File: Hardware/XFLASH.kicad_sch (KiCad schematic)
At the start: 0 parts

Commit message: Checkpoint
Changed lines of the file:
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@@
 (kicad_sch (version 20230121) (generator eeschema)
   (paper "A4")
-  (hierarchical_label "SCK" (shape input) (at 127 35.56 0) (fields_autoplaced)
+  (bus (pts (xy 241.3 25.4) (xy 266.7 25.4))
+    (stroke (width 0) (type default))
+  )
+  (label "IO[0..3]" (at 241.3 25.4 0) (fields_autoplaced)
+    (effects (font (size 1.27 1.27)) (justify left bottom))
+  )
+  (hierarchical_label "CLK" (shape input) (at 127 35.56 0) (fields_autoplaced)
     (effects (font (size 1.27 1.27)) (justify left))
   )
-  (hierarchical_label "IO1" (shape bidirectional) (at 127 43.18 0) (fields_autoplaced)
+  (hierarchical_label "VCC" (shape passive) (at 127 45.72 0) (fields_autoplaced)
     (effects (font (size 1.27 1.27)) (justify left))
   )
-  (hierarchical_label "IO3" (shape bidirectional) (at 127 48.26 0) (fields_autoplaced)
+  (hierarchical_label "IO[0..3]" (shape bidirectional) (at 266.7 25.4 0) (fields_autoplaced)
     (effects (font (size 1.27 1.27)) (justify left))
   )
-  (hierarchical_label "IO0" (shape bidirectional) (at 127 40.64 0) (fields_autoplaced)
+  (hierarchical_label "~{CS}" (shape input) (at 127 38.1 0) (fields_autoplaced)
     (effects (font (size 1.27 1.27)) (justify left))
   )
-  (hierarchical_label "~{NSS}" (shape input) (at 127 38.1 0) (fields_autoplaced)
-    (effects (font (size 1.27 1.27)) (justify left))
-  )
-  (hierarchical_label "IO2" (shape bidirectional) (at 127 45.72 0) (fields_autoplaced)
-    (effects (font (size 1.27 1.27)) (justify left))
-  )

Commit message: Checkpoint
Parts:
- added C25: 100nF, symbol Device:C_Small
- added R18, R19, R20: 10K, symbol Device:R_Small
- added U6: IS25LP064A-JBLE, Package_SO:SOIC-8_5.23x5.23mm_P1.27mm, symbol Memory_Flash:W25Q128JVS
- added U8: W25Q128JVPM, Package_SON:WSON-8-1EP_6x5mm_P1.27mm_EP3.4x4.3mm, symbol Memory_Flash:W25Q32JVZP
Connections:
- net CLK: now also U6.6 (CLK), U8.6 (CLK)
- net VCC: now also C25.1, R18.1, R19.1, R20.1, U6.8 (VCC), U8.8 (VCC)
- net ~{CS}: now also R18.2, U6.1 (~{CS}), U8.1 (~{CS})
- new net GND: C25.2, U6.4 (GND), U8.4 (GND), U8.9 (EP)
- new net IO0: U6.5 (DI(IO0)), U8.5 (DI(IO0))
- new net IO1: U6.2 (DO(IO1)), U8.2 (DO(IO1))
- new net IO2: R19.2, U6.3 (IO2), U8.3 (IO2)
- new net IO3: R20.2, U6.7 (IO3), U8.7 (IO3)

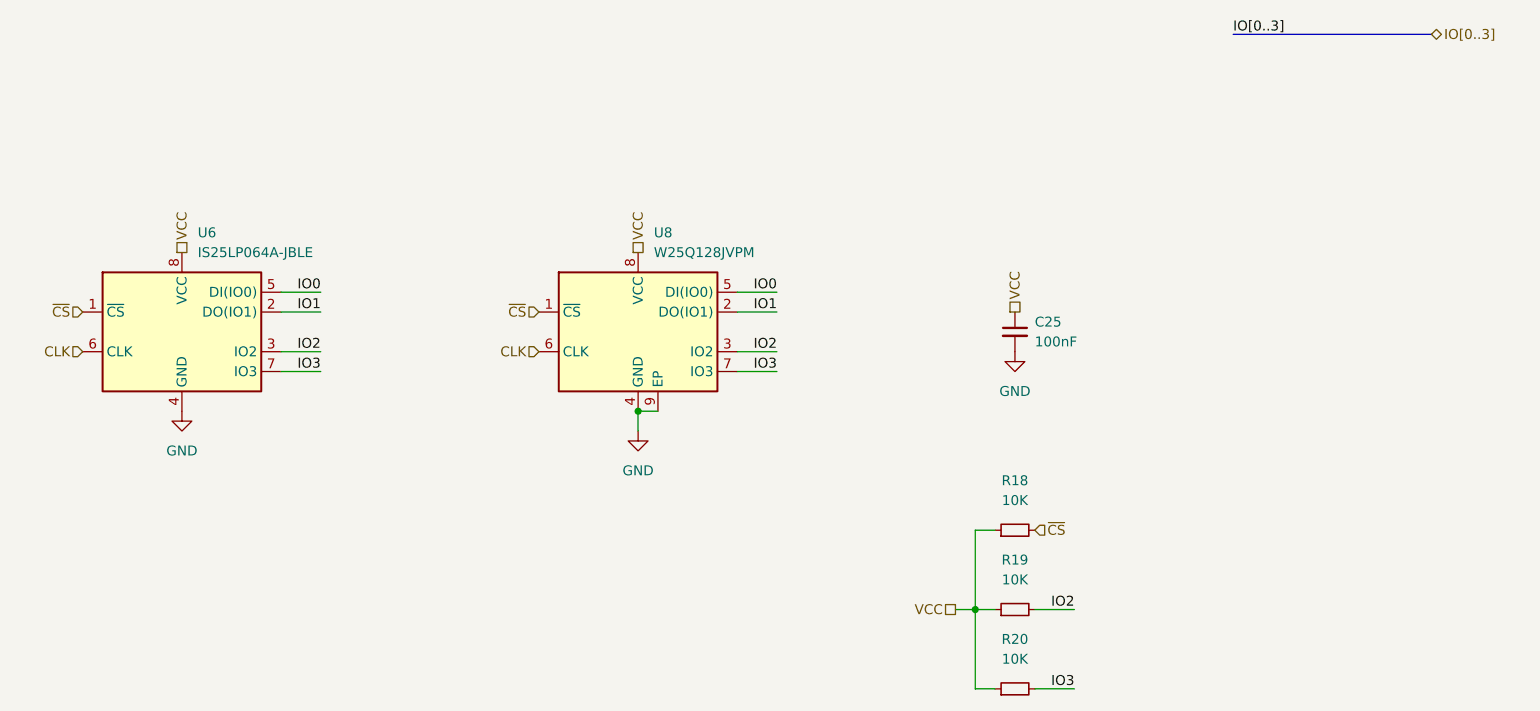
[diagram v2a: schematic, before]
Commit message: Add stacked footprints graphic
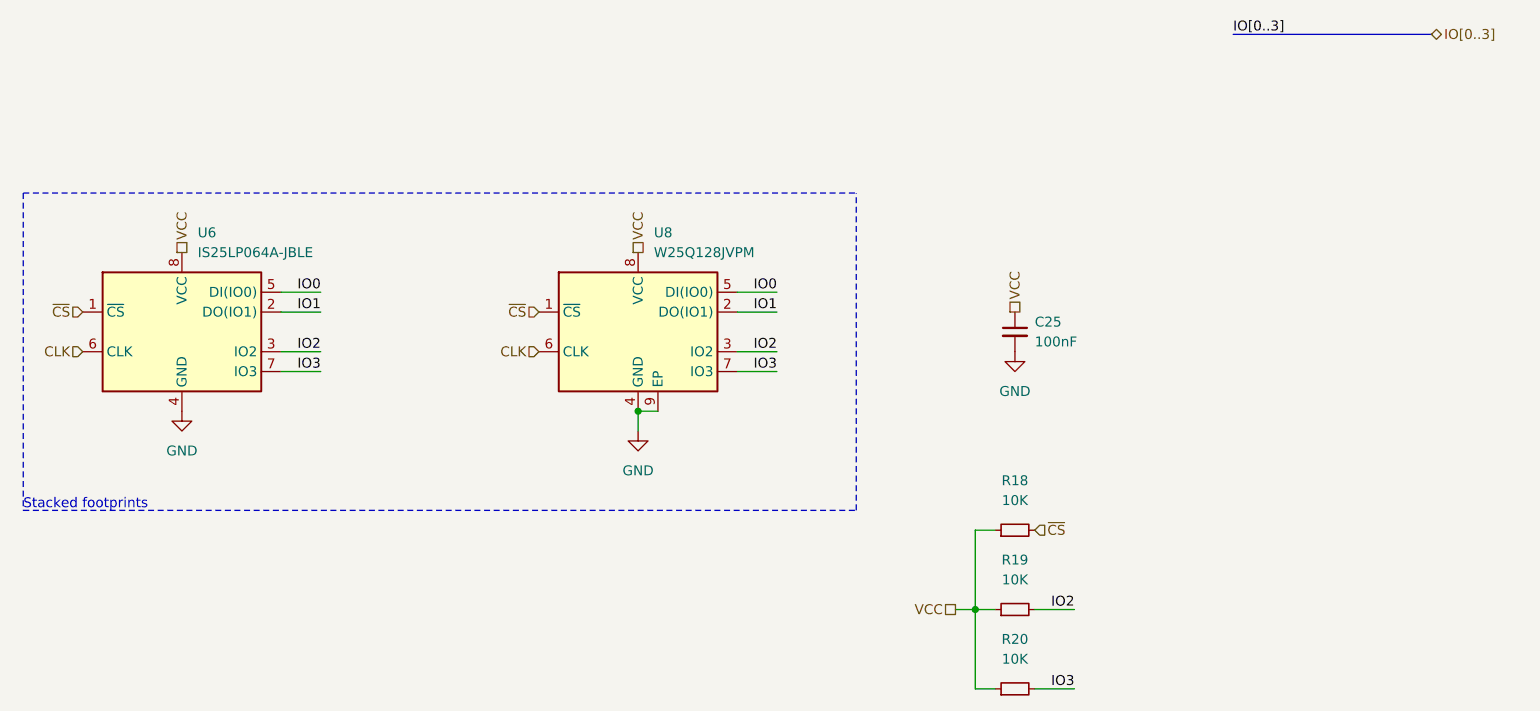
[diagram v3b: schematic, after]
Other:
- note added: "Stacked footprints"
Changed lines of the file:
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@@
   (junction (at 165.1 73.66) (diameter 0) (color 0 0 0 0)
+  )
+  (polyline (pts (xy 193.04 86.36) (xy 193.04 45.72))
+    (stroke (width 0) (type dash))
   )
   (wire (pts (xy 208.28 109.22) (xy 210.82 109.22))
@@
     (stroke (width 0) (type default))
   )
+  (polyline (pts (xy 86.36 45.72) (xy 86.36 86.36))
+    (stroke (width 0) (type dash))
+  )
   (wire (pts (xy 208.28 88.9) (xy 210.82 88.9))
     (stroke (width 0) (type default))
@@
   (wire (pts (xy 165.1 73.66) (xy 165.1 76.2))
     (stroke (width 0) (type default))
+  )
+  (polyline (pts (xy 86.36 86.36) (xy 193.04 86.36))
+    (stroke (width 0) (type dash))
   )
   (wire (pts (xy 215.9 99.06) (xy 220.98 99.06))
@@
   (bus (pts (xy 241.3 25.4) (xy 266.7 25.4))
     (stroke (width 0) (type default))
+  )
+  (polyline (pts (xy 86.36 45.72) (xy 193.04 45.72))
+    (stroke (width 0) (type dash))
   )
   (wire (pts (xy 208.28 99.06) (xy 208.28 109.22))
@@
     (stroke (width 0) (type default))
   )
+  (text "Stacked footprints" (at 86.36 86.36 0)
+    (effects (font (size 1.27 1.27)) (justify left bottom))
+  )
   (label "IO2" (at 220.98 99.06 180) (fields_autoplaced)

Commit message: ERC fixes
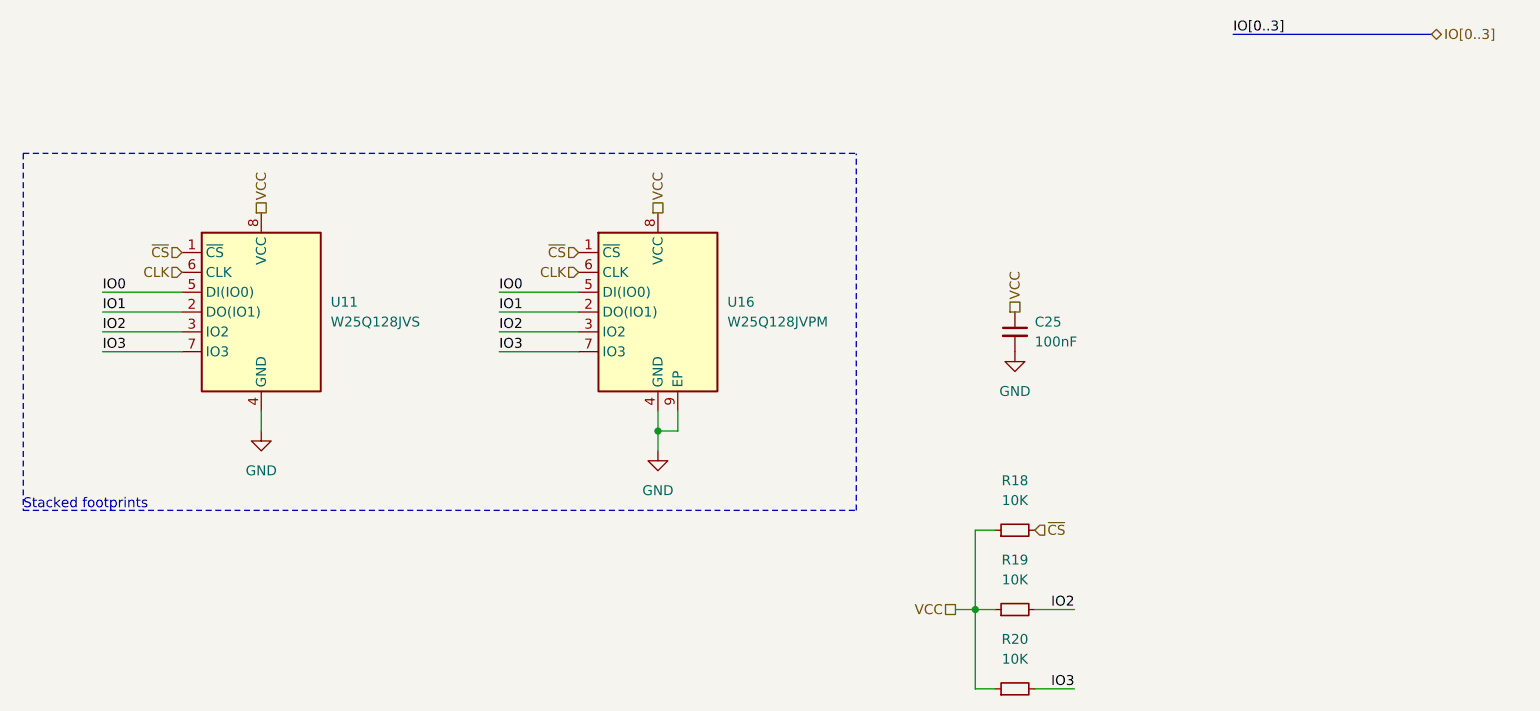
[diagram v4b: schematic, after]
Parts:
- removed U6: IS25LP064A-JBLE, Package_SO:SOIC-8_5.23x5.23mm_P1.27mm, symbol Memory_Flash:W25Q128JVS
- removed U8: W25Q128JVPM, Package_SON:WSON-8-1EP_6x5mm_P1.27mm_EP3.4x4.3mm, symbol Memory_Flash:W25Q32JVZP
- added U11: W25Q128JVS, Package_SO:SOIC-8_5.23x5.23mm_P1.27mm, symbol Memory_Flash:W25Q128JVS
- added U16: W25Q128JVPM, Package_SON:WSON-8-1EP_6x5mm_P1.27mm_EP3.4x4.3mm, symbol Memory_Flash:W25Q32JVZP
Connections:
- net CLK: now also U11.6 (CLK), U16.6 (CLK)
- net GND: now also U11.4 (GND), U16.4 (GND), U16.9 (EP)
- net IO0: now also U11.5 (DI(IO0)), U16.5 (DI(IO0))
- net IO1: now also U11.2 (DO(IO1)), U16.2 (DO(IO1))
- net IO2: now also U11.3 (IO2), U16.3 (IO2)
- net IO3: now also U11.7 (IO3), U16.7 (IO3)
- net VCC: now also U11.8 (VCC), U16.8 (VCC)
- net ~{CS}: now also U11.1 (~{CS}), U16.1 (~{CS})

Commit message: Checkpoint
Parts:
- renumbered C25 to C?, R20 to R?, R18 to R?, R19 to R?, U11 to U501, U16 to U502
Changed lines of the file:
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@@
   (symbol (lib_id "Device:R_Small") (at 213.36 109.22 90) (unit 1)
     (in_bom yes) (on_board yes) (dnp no) (fields_autoplaced)
-    (property "Reference" "R20" (at 213.36 102.87 90)
+    (property "Reference" "R?" (at 213.36 102.87 90)
       (effects (font (size 1.27 1.27)))
     )
@@
       (project "STM32_144_dev_board1"
         (path "/687cb9d5-0148-4d02-92a8-2c8817ac4452/5a3f2e83-2524-4987-84b3-442c172b4877"
-          (reference "R20") (unit 1)
-        )
-      )
-      (project "Avionus_Flight_Controller"
-        (path "/ddc7e940-0588-4587-8902-8ced9e615ace/31e99b3b-1804-434d-b69d-c6e432b73a14"
-          (reference "R62") (unit 1)
-        )
-        (path "/ddc7e940-0588-4587-8902-8ced9e615ace/5d37de1e-dde8-47f7-bd31-55135827514e"
-          (reference "R65") (unit 1)
+          (reference "R?") (unit 1)
+        )
+      )
+      (project "Avionus_Flight_Controller"
+        (path "/ddc7e940-0588-4587-8902-8ced9e615ace/31e99b3b-1804-434d-b69d-c6e432b73a14"
+          (reference "R503") (unit 1)
+        )
+        (path "/ddc7e940-0588-4587-8902-8ced9e615ace/5d37de1e-dde8-47f7-bd31-55135827514e"
+          (reference "R603") (unit 1)
         )
       )
@@
   (symbol (lib_id "Device:C_Small") (at 213.36 63.5 0) (unit 1)
     (in_bom yes) (on_board yes) (dnp no) (fields_autoplaced)
-    (property "Reference" "C25" (at 215.9 62.2362 0)
+    (property "Reference" "C?" (at 215.9 62.2362 0)
       (effects (font (size 1.27 1.27)) (justify left))
     )
@@
       (project "STM32_144_dev_board1"
         (path "/687cb9d5-0148-4d02-92a8-2c8817ac4452/5a3f2e83-2524-4987-84b3-442c172b4877"
-          (reference "C25") (unit 1)
-        )
-      )
-      (project "Avionus_Flight_Controller"
-        (path "/ddc7e940-0588-4587-8902-8ced9e615ace/31e99b3b-1804-434d-b69d-c6e432b73a14"
-          (reference "C25") (unit 1)
-        )
-        (path "/ddc7e940-0588-4587-8902-8ced9e615ace/5d37de1e-dde8-47f7-bd31-55135827514e"
-          (reference "C26") (unit 1)
+          (reference "C?") (unit 1)
+        )
+      )
+      (project "Avionus_Flight_Controller"
+        (path "/ddc7e940-0588-4587-8902-8ced9e615ace/31e99b3b-1804-434d-b69d-c6e432b73a14"
+          (reference "C501") (unit 1)
+        )
+        (path "/ddc7e940-0588-4587-8902-8ced9e615ace/5d37de1e-dde8-47f7-bd31-55135827514e"
+          (reference "C601") (unit 1)
         )
       )
@@
   (symbol (lib_id "Memory_Flash:W25Q128JVS") (at 116.84 60.96 0) (unit 1)
     (in_bom yes) (on_board yes) (dnp no) (fields_autoplaced)
-    (property "Reference" "U11" (at 125.73 59.69 0)
+    (property "Reference" "U501" (at 125.73 59.69 0)
       (effects (font (size 1.27 1.27)) (justify left))
     )
@@
       (project "Avionus_Flight_Controller"
         (path "/ddc7e940-0588-4587-8902-8ced9e615ace/31e99b3b-1804-434d-b69d-c6e432b73a14"
-          (reference "U11") (unit 1)
-        )
-        (path "/ddc7e940-0588-4587-8902-8ced9e615ace/5d37de1e-dde8-47f7-bd31-55135827514e"
-          (reference "U13") (unit 1)
+          (reference "U501") (unit 1)
+        )
+        (path "/ddc7e940-0588-4587-8902-8ced9e615ace/5d37de1e-dde8-47f7-bd31-55135827514e"
+          (reference "U601") (unit 1)
         )
       )
@@
   (symbol (lib_name "GND_1") (lib_id "power:GND") (at 116.84 76.2 0) (unit 1)
     (in_bom yes) (on_board yes) (dnp no) (fields_autoplaced)
-    (property "Reference" "#PWR037" (at 116.84 82.55 0)
+    (property "Reference" "#PWR0501" (at 116.84 82.55 0)
       (effects (font (size 1.27 1.27)) hide)
     )
@@
       (project "Avionus_Flight_Controller"
         (path "/ddc7e940-0588-4587-8902-8ced9e615ace/31e99b3b-1804-434d-b69d-c6e432b73a14"
-          (reference "#PWR037") (unit 1)
-        )
-        (path "/ddc7e940-0588-4587-8902-8ced9e615ace/5d37de1e-dde8-47f7-bd31-55135827514e"
-          (reference "#PWR039") (unit 1)
+          (reference "#PWR0501") (unit 1)
+        )
+        (path "/ddc7e940-0588-4587-8902-8ced9e615ace/5d37de1e-dde8-47f7-bd31-55135827514e"
+          (reference "#PWR0601") (unit 1)
         )
       )
@@
   (symbol (lib_id "Device:R_Small") (at 213.36 88.9 90) (unit 1)
     (in_bom yes) (on_board yes) (dnp no) (fields_autoplaced)
-    (property "Reference" "R18" (at 213.36 82.55 90)
+    (property "Reference" "R?" (at 213.36 82.55 90)
       (effects (font (size 1.27 1.27)))
     )
@@
       (project "STM32_144_dev_board1"
         (path "/687cb9d5-0148-4d02-92a8-2c8817ac4452/5a3f2e83-2524-4987-84b3-442c172b4877"
-          (reference "R18") (unit 1)
-        )
-      )
-      (project "Avionus_Flight_Controller"
-        (path "/ddc7e940-0588-4587-8902-8ced9e615ace/31e99b3b-1804-434d-b69d-c6e432b73a14"
-          (reference "R60") (unit 1)
-        )
-        (path "/ddc7e940-0588-4587-8902-8ced9e615ace/5d37de1e-dde8-47f7-bd31-55135827514e"
-          (reference "R63") (unit 1)
+          (reference "R?") (unit 1)
+        )
+      )
+      (project "Avionus_Flight_Controller"
+        (path "/ddc7e940-0588-4587-8902-8ced9e615ace/31e99b3b-1804-434d-b69d-c6e432b73a14"
+          (reference "R501") (unit 1)
+        )
+        (path "/ddc7e940-0588-4587-8902-8ced9e615ace/5d37de1e-dde8-47f7-bd31-55135827514e"
+          (reference "R601") (unit 1)
         )
       )
@@
   (symbol (lib_id "power:GND") (at 213.36 66.04 0) (unit 1)
     (in_bom yes) (on_board yes) (dnp no) (fields_autoplaced)
-    (property "Reference" "#PWR038" (at 213.36 72.39 0)
+    (property "Reference" "#PWR0503" (at 213.36 72.39 0)
       (effects (font (size 1.27 1.27)) hide)
     )
@@
       (project "Avionus_Flight_Controller"
         (path "/ddc7e940-0588-4587-8902-8ced9e615ace/31e99b3b-1804-434d-b69d-c6e432b73a14"
-          (reference "#PWR038") (unit 1)
-        )
-        (path "/ddc7e940-0588-4587-8902-8ced9e615ace/5d37de1e-dde8-47f7-bd31-55135827514e"
-          (reference "#PWR042") (unit 1)
+          (reference "#PWR0503") (unit 1)
+        )
+        (path "/ddc7e940-0588-4587-8902-8ced9e615ace/5d37de1e-dde8-47f7-bd31-55135827514e"
+          (reference "#PWR0603") (unit 1)
         )
       )
@@
   (symbol (lib_name "W25Q32JVZP_1") (lib_id "Memory_Flash:W25Q32JVZP") (at 167.64 60.96 0) (unit 1)
     (in_bom yes) (on_board yes) (dnp no) (fields_autoplaced)
-    (property "Reference" "U16" (at 176.53 59.69 0)
+    (property "Reference" "U502" (at 176.53 59.69 0)
       (effects (font (size 1.27 1.27)) (justify left))
     )
@@
       (project "Avionus_Flight_Controller"
         (path "/ddc7e940-0588-4587-8902-8ced9e615ace/31e99b3b-1804-434d-b69d-c6e432b73a14"
-          (reference "U16") (unit 1)
-        )
-        (path "/ddc7e940-0588-4587-8902-8ced9e615ace/5d37de1e-dde8-47f7-bd31-55135827514e"
-          (reference "U17") (unit 1)
+          (reference "U502") (unit 1)
+        )
+        (path "/ddc7e940-0588-4587-8902-8ced9e615ace/5d37de1e-dde8-47f7-bd31-55135827514e"
+          (reference "U602") (unit 1)
         )
       )
@@
   (symbol (lib_name "GND_1") (lib_id "power:GND") (at 167.64 78.74 0) (unit 1)
     (in_bom yes) (on_board yes) (dnp no) (fields_autoplaced)
-    (property "Reference" "#PWR041" (at 167.64 85.09 0)
+    (property "Reference" "#PWR0502" (at 167.64 85.09 0)
       (effects (font (size 1.27 1.27)) hide)
     )
@@
       (project "Avionus_Flight_Controller"
         (path "/ddc7e940-0588-4587-8902-8ced9e615ace/31e99b3b-1804-434d-b69d-c6e432b73a14"
-          (reference "#PWR041") (unit 1)
-        )
-        (path "/ddc7e940-0588-4587-8902-8ced9e615ace/5d37de1e-dde8-47f7-bd31-55135827514e"
-          (reference "#PWR043") (unit 1)
+          (reference "#PWR0502") (unit 1)
+        )
+        (path "/ddc7e940-0588-4587-8902-8ced9e615ace/5d37de1e-dde8-47f7-bd31-55135827514e"
+          (reference "#PWR0602") (unit 1)
         )
       )
@@
   (symbol (lib_id "Device:R_Small") (at 213.36 99.06 90) (unit 1)
     (in_bom yes) (on_board yes) (dnp no) (fields_autoplaced)
-    (property "Reference" "R19" (at 213.36 92.71 90)
+    (property "Reference" "R?" (at 213.36 92.71 90)
       (effects (font (size 1.27 1.27)))
     )
@@
       (project "STM32_144_dev_board1"
         (path "/687cb9d5-0148-4d02-92a8-2c8817ac4452/5a3f2e83-2524-4987-84b3-442c172b4877"
-          (reference "R19") (unit 1)
-        )
-      )
-      (project "Avionus_Flight_Controller"
-        (path "/ddc7e940-0588-4587-8902-8ced9e615ace/31e99b3b-1804-434d-b69d-c6e432b73a14"
-          (reference "R61") (unit 1)
-        )
-        (path "/ddc7e940-0588-4587-8902-8ced9e615ace/5d37de1e-dde8-47f7-bd31-55135827514e"
-          (reference "R64") (unit 1)
-        )
-      )
+          (reference "R?") (unit 1)
+        )
+      )
+      (project "Avionus_Flight_Controller"
+        (path "/ddc7e940-0588-4587-8902-8ced9e615ace/31e99b3b-1804-434d-b69d-c6e432b73a14"
+          (reference "R502") (unit 1)
+        )
+        (path "/ddc7e940-0588-4587-8902-8ced9e615ace/5d37de1e-dde8-47f7-bd31-55135827514e"
+          (reference "R602") (unit 1)
+        )
+      )

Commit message: Checkpoint
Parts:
- C?: footprint (none) -> Capacitor_SMD:C_0603_1608Metric
- R? (x3): footprint (none) -> Resistor_SMD:R_0603_1608Metric
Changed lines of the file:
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@@
       (effects (font (size 1.27 1.27)))
     )
-    (property "Footprint" "" (at 213.36 109.22 0)
+    (property "Footprint" "Resistor_SMD:R_0603_1608Metric" (at 213.36 109.22 0)
       (effects (font (size 1.27 1.27)) hide)
     )
@@
       (effects (font (size 1.27 1.27)) (justify left))
     )
-    (property "Footprint" "" (at 213.36 63.5 0)
+    (property "Footprint" "Capacitor_SMD:C_0603_1608Metric" (at 213.36 63.5 0)
       (effects (font (size 1.27 1.27)) hide)
     )
@@
       (effects (font (size 1.27 1.27)))
     )
-    (property "Footprint" "" (at 213.36 88.9 0)
+    (property "Footprint" "Resistor_SMD:R_0603_1608Metric" (at 213.36 88.9 0)
       (effects (font (size 1.27 1.27)) hide)
     )
@@
       (effects (font (size 1.27 1.27)))
     )
-    (property "Footprint" "" (at 213.36 99.06 0)
-      (effects (font (size 1.27 1.27)) hide)
-    )
+    (property "Footprint" "Resistor_SMD:R_0603_1608Metric" (at 213.36 99.06 0)
+      (effects (font (size 1.27 1.27)) hide)
+    )

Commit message: Finalize silkscreen
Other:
- title: (none) -> Avionus_Flight_Controller
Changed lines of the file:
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@@
 (kicad_sch (version 20230121) (generator eeschema)
   (paper "A4")
+  (title_block
+    (title "Avionus_Flight_Controller")
+    (date "2023-11-25")
+    (rev "1.0")
+  )
   (junction (at 167.64 76.2) (diameter 0) (color 0 0 0 0)
   )
